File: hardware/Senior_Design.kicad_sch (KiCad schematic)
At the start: 0 parts

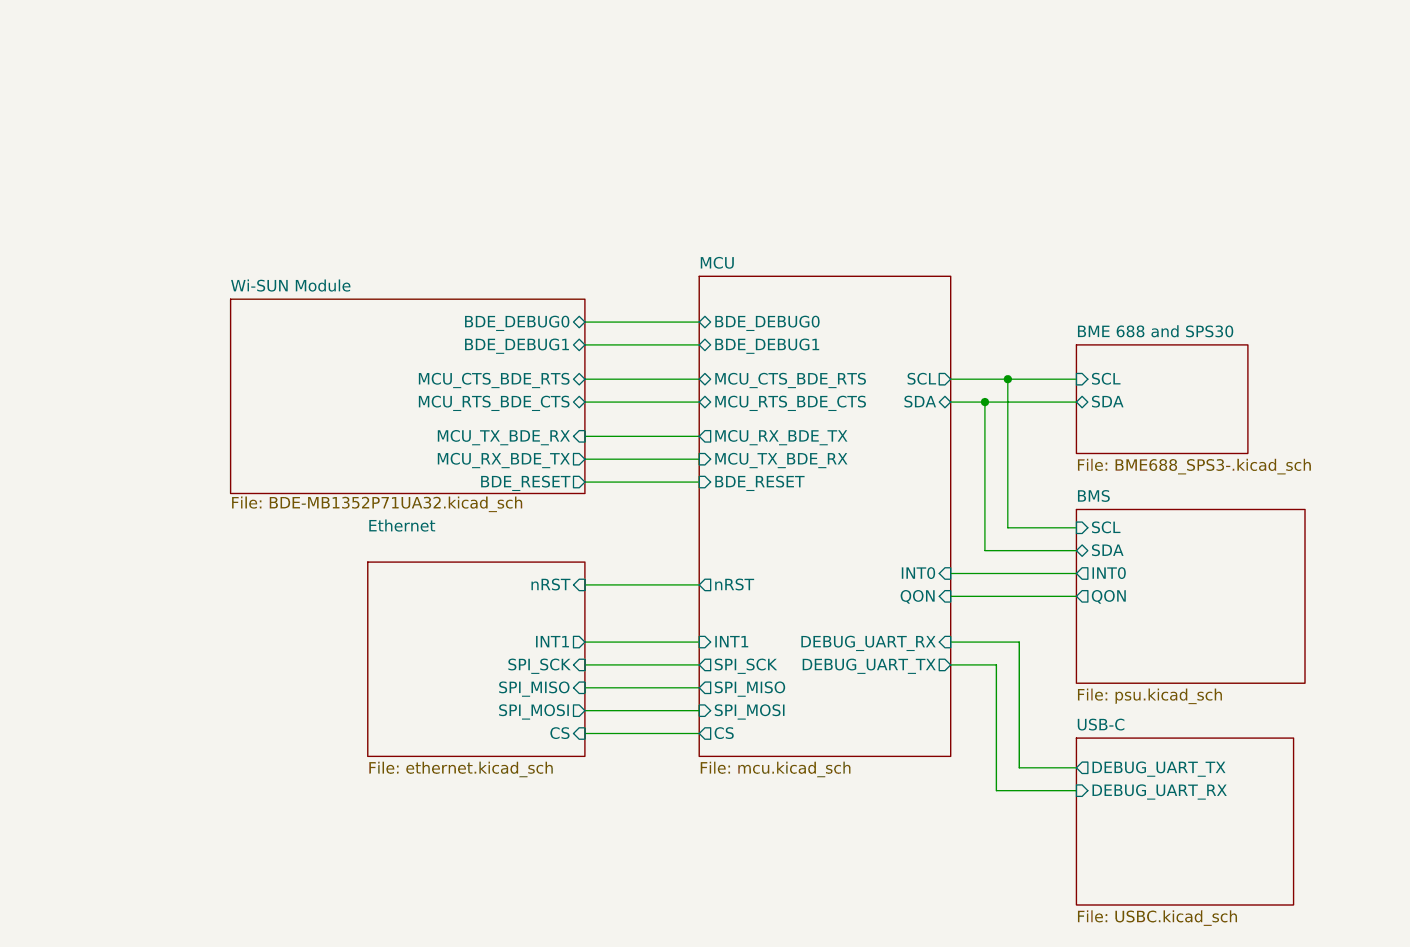
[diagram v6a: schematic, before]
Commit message: updated labels
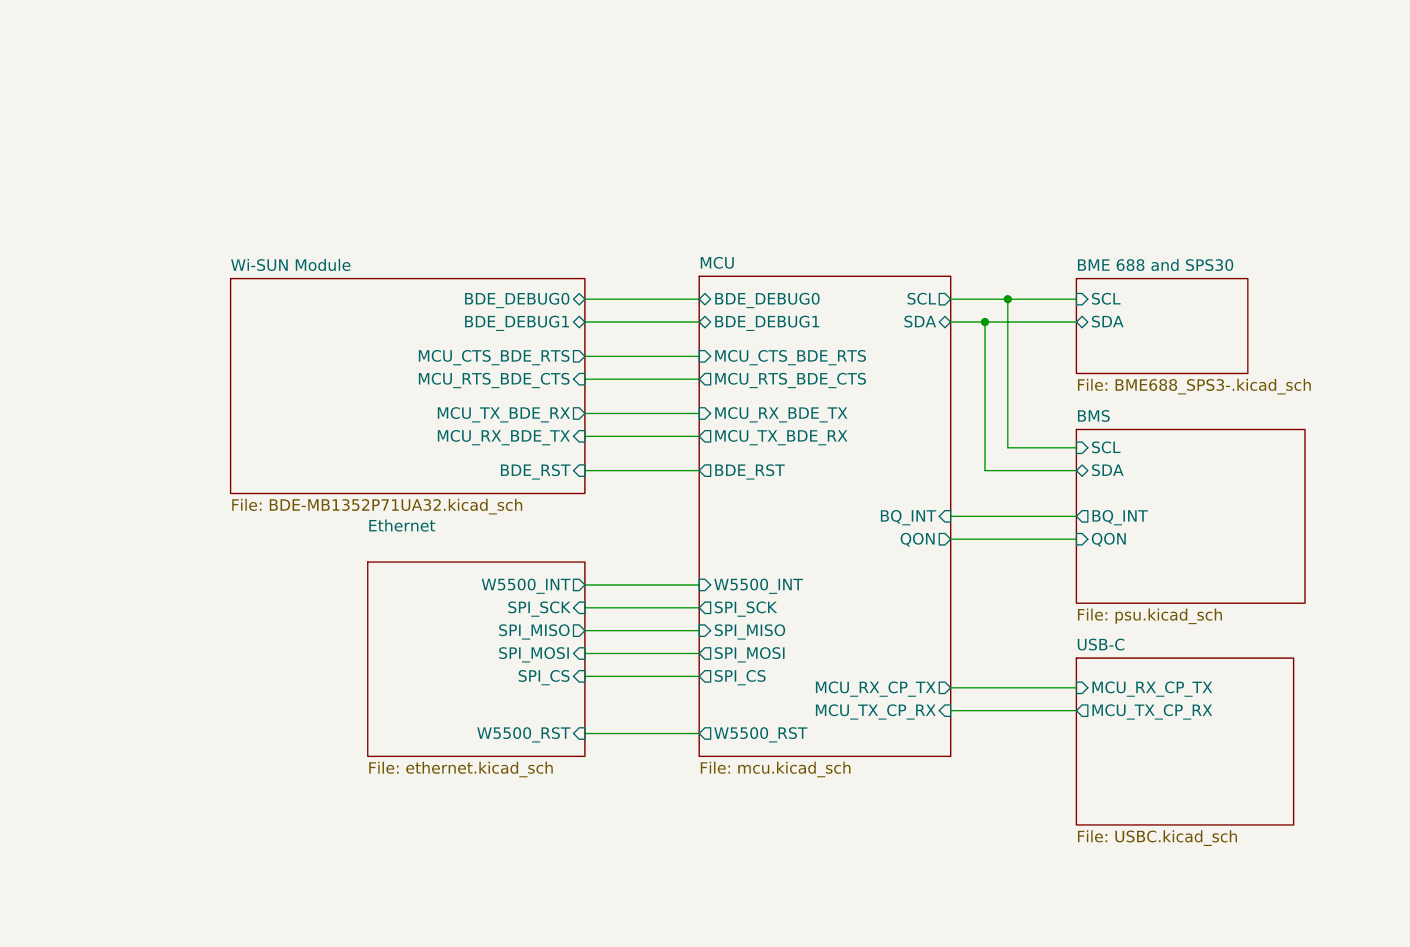
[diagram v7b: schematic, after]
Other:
- sheet BMS ports: added BQ_INT; removed INT0
- sheet Ethernet ports: added SPI_CS, W5500_INT, W5500_RST; removed CS, INT1, nRST
- sheet MCU ports: added BDE_RST, BQ_INT, MCU_RX_CP_TX, MCU_TX_CP_RX, SPI_CS, W5500_INT, W5500_RST; removed BDE_RESET, CS, DEBUG_UART_RX, DEBUG_UART_TX, INT0, INT1, nRST
- sheet USB-C ports: added MCU_RX_CP_TX, MCU_TX_CP_RX; removed DEBUG_UART_RX, DEBUG_UART_TX
- sheet Wi-SUN Module ports: added BDE_RST; removed BDE_RESET
